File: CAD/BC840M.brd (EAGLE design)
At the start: 25.5 x 40 mm, 79 parts, among them J1 SM02B-SRSS-TB(LF)(SN), U2 BC840M, U3 LP5907MFX-3.3/NOPB, U4 LP5907MFX-3.3/NOPB, U5 ADS131M08IPBS, X1 ABM3B-8.000MHZ-B2-T, X2 FC-12M

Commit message: Update BC840M.brd
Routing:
- net GND: vias 26 -> 27
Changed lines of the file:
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@@
 <wire x1="22.0208" y1="32.121459375" x2="22.0208" y2="31.765859375" width="0.1524" layer="1"/>
 <via x="31.968440625" y="31.4071" extent="1-16" drill="0.2"/>
+<via x="20.26158125" y="38.3794" extent="1-16" drill="0.2"/>
 <wire x1="33.683209375" y1="67.39101875" x2="33.578796875" y2="67.39101875" width="0" layer="19" extent="16-16"/>
 <wire x1="33.61181875" y1="68.78828125" x2="32.953959375" y2="68.072" width="0" layer="19" extent="1-1"/>
 <wire x1="29.0550625" y1="58.625734375" x2="30.4217" y2="58.841640625" width="0" layer="19" extent="16-16"/>
 <wire x1="27.3264" y1="34.6328" x2="25.6996" y2="35.3822" width="0" layer="19" extent="1-1"/>
+<wire x1="25.583003125" y1="49.0982" x2="27.4828" y2="48.8269" width="0" layer="19" extent="1-1"/>
 </signal>
 <signal name="XTAL2_2">

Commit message: latest
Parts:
- added C26, C9: 4.7uF, standardparts:0201
- added C27: 0.1uF, standardparts:0201
- added R28, R29: 10kΩ, standardparts:0402
- added SJ2: (no value), jumper:SJ
- R1: value 46.4kΩ -> 10kΩ
- R3, R4: device standardparts:0201 -> standardparts:0603
- moved R1 2.40 mm to (25.2, 35.7), turned to 270 degrees
- moved C8 1.75 mm to (30.8, 57.1)
- moved C5 1.70 mm to (30.9, 56.3)
- moved C14 1.35 mm to (24.2, 36.0)
- moved R4 1.21 mm to (27.7, 36.8), turned to 180 degrees
- moved R2 0.78 mm to (22.1, 56.2)
- moved R3 0.69 mm to (30.7, 34.4)
- moved C19 0.54 mm to (18.0, 36.9)
- moved C18 0.48 mm to (17.9, 37.7)
- moved S1 0.44 mm to (27.7, 39.6)
- moved SJ1 0.39 mm to (33.2, 57.4)
- moved U$3 0.38 mm to (19.1, 36.4)
- moved C10 0.35 mm to (28.1, 35.7), turned to 180 degrees
- moved C11 0.29 mm to (30.2, 33.0)
- moved R5 0.28 mm to (13.7, 38.3)
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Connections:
- net P4 renamed CUR_DETECT
- net XTAL1_2 renamed CLKIN
- removed net N$67: U$2.3
- removed net REFIN: U5.14
- removed net TD: U$2.15
- removed net TMR: R1.1
- removed net VDDH: U2.A7
- removed net XTAL2_2: C4.1, U5.22, X1.3
- new net CLKOUT: C4.1, JP3.1, U5.22, X1.3
- net +5V: now also C9.2
- net +5V_ISO: now also C26.2, C27.2
- net AVDD: now also SJ2.1, SJ2.2
- net BAT: now also U$2.3
- net CHG: now also R29.2
- net DIN: now also JP3.19
- net DOUT: now also JP3.17
- net GND: now also C26.1, C27.1, C9.1, JP3.5, R1.1, U$2.15, U5.14; no longer R1.2
- net P101: now also JP2.8
- net P104: now also JP2.10
- net P106: now also JP3.11
- net P107: now also JP2.14
- net P108: now also JP2.13
- net P109: now also JP2.15
- net P11: now also JP2.5
- net P110: now also JP3.18
- net P111: now also JP3.4
- net P113: now also JP3.6
- net P114: now also JP3.8
- net P12: now also JP2.9
- net P14: now also JP2.1
- net P15: now also JP2.2
- net P17: now also JP2.3
- net P19: now also JP2.19
- net P2: now also JP3.14
- net P21: now also JP2.12
- net P22: now also JP2.6
- net P23: now also JP3.13
- net P24: now also JP3.20
- net P25: now also JP2.4
- net P28: now also JP3.2
- net P29: now also JP3.16
- net P3: now also JP3.9
- net P30: now also JP3.7
- net P31: now also JP3.12
- net P5: now also JP3.10
- net P7: now also JP2.11
- net P8: now also JP2.7
- net PGOOD: now also R28.2
- net RESET: now also JP2.17
- net SCLK: now also JP3.15
- net SWDCLK: now also JP2.18
- net SWDIO: now also JP2.16
- net SWO: now also JP2.20
- net TS: now also R1.2
- net VDD: now also R28.1, R29.1, U2.A7
- net VIN: now also JP3.3
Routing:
- net GND: track 97.3 -> 129.2 mm
- net VDD: track 58.4 -> 80.7 mm
- net CLKOUT: track 0.00 -> 18.5 mm, vias 0 -> 1
- net XTAL2_2: track 16.8 -> 0.00 mm, vias 1 -> 0
- net P11: track 13.2 -> 18.9 mm
- net BAT: track 26.1 -> 30.0 mm
- net VIN: track 50.7 -> 46.9 mm
- net TS: track 0.00 -> 3.38 mm
- net +5V_ISO: track 66.5 -> 69.5 mm
- net VSWITCH: track 29.0 -> 26.1 mm
- net P7: track 6.62 -> 8.50 mm
- net P113: track 20.1 -> 22.0 mm
- net P114: track 15.5 -> 17.2 mm
- net SCLK: track 29.5 -> 31.1 mm
- net P21: track 22.1 -> 23.7 mm
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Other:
- board text added: "R2"
- board text added: "S1"

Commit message: touchups
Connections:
- net VDD: now also JP3.3
- net VIN: no longer JP3.3
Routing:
- net VIN: track 46.9 -> 35.0 mm
- net VDD: track 80.7 -> 85.2 mm, vias 2 -> 3
- net P28: track 26.9 -> 28.5 mm
- net P111: track 26.5 -> 28.0 mm
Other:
- board text added: "101"
- board text added: "104"
- board text added: "106"
- board text added: "107"
- board text added: "108"
- board text added: "109"
- board text added: "11"
- board text added: "110"
- board text added: "111"
- board text added: "113"
- board text added: "114"
- board text added: "12"
- board text added: "14"
- board text added: "15"
- board text added: "17"
- board text added: "19"
- board text added: "2"
- board text added: "21"
- board text added: "22"
- board text added: "23"
- board text added: "24"
- board text added: "25"
- board text added: "28"
- board text added: "29"
- board text added: "3"
- board text added: "30"
- board text added: "31"
- board text added: "5"
- board text added: "7"
- board text added: "8"
- board text added: "8.192M"
- board text added: "BC840M"
- board text added: "DIN"
- board text added: "DOUT"
- board text added: "SCLK"
- board text added: "SWD CLK"
- board text added: "SWD IO"

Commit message: Update BC840M.brd
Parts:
- moved R6 0.36 mm to (22.4, 40.9)
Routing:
- net GND: track 129.2 -> 158.6 mm

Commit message: _
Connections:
- removed net N$76: U$2.11
- net VSWITCH: now also U$2.11
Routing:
- net VSWITCH: track 26.1 -> 27.7 mm
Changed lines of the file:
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@@
 <grid distance="0.1" unitdist="mil" unit="mil" style="lines" multiple="1" display="no" altdistance="5" altunitdist="mil" altunit="mil"/>
 <layers>
-<layer number="1" name="Top" color="4" fill="1" visible="no" active="yes"/>
+<layer number="1" name="Top" color="4" fill="1" visible="yes" active="yes"/>
 <layer number="2" name="Route2" color="16" fill="1" visible="no" active="no"/>
 <layer number="3" name="Route3" color="17" fill="1" visible="no" active="no"/>
@@
 <layer number="14" name="Route14" color="22" fill="1" visible="no" active="no"/>
 <layer number="15" name="Route15" color="23" fill="1" visible="no" active="no"/>
-<layer number="16" name="Bottom" color="1" fill="1" visible="yes" active="yes"/>
+<layer number="16" name="Bottom" color="1" fill="1" visible="no" active="yes"/>
 <layer number="17" name="Pads" color="2" fill="1" visible="yes" active="yes"/>
 <layer number="18" name="Vias" color="2" fill="1" visible="yes" active="yes"/>
 <layer number="19" name="Unrouted" color="6" fill="1" visible="yes" active="yes"/>
 <layer number="20" name="Dimension" color="24" fill="1" visible="yes" active="yes"/>
-<layer number="21" name="tPlace" color="7" fill="1" visible="no" active="yes"/>
-<layer number="22" name="bPlace" color="7" fill="1" visible="yes" active="yes"/>
-<layer number="23" name="tOrigins" color="15" fill="1" visible="no" active="yes"/>
-<layer number="24" name="bOrigins" color="15" fill="1" visible="yes" active="yes"/>
-<layer number="25" name="tNames" color="7" fill="1" visible="no" active="yes"/>
-<layer number="26" name="bNames" color="7" fill="1" visible="yes" active="yes"/>
+<layer number="21" name="tPlace" color="7" fill="1" visible="yes" active="yes"/>
+<layer number="22" name="bPlace" color="7" fill="1" visible="no" active="yes"/>
+<layer number="23" name="tOrigins" color="15" fill="1" visible="yes" active="yes"/>
+<layer number="24" name="bOrigins" color="15" fill="1" visible="no" active="yes"/>
+<layer number="25" name="tNames" color="7" fill="1" visible="yes" active="yes"/>
+<layer number="26" name="bNames" color="7" fill="1" visible="no" active="yes"/>
 <layer number="27" name="tValues" color="7" fill="1" visible="no" active="yes"/>
 <layer number="28" name="bValues" color="7" fill="1" visible="no" active="yes"/>
@@
 <layer number="37" name="tTest" color="7" fill="1" visible="no" active="yes"/>
 <layer number="38" name="bTest" color="7" fill="1" visible="no" active="yes"/>
-<layer number="39" name="tKeepout" color="4" fill="11" visible="no" active="yes"/>
-<layer number="40" name="bKeepout" color="1" fill="11" visible="yes" active="yes"/>
-<layer number="41" name="tRestrict" color="4" fill="10" visible="no" active="yes"/>
-<layer number="42" name="bRestrict" color="1" fill="10" visible="yes" active="yes"/>
+<layer number="39" name="tKeepout" color="4" fill="11" visible="yes" active="yes"/>
+<layer number="40" name="bKeepout" color="1" fill="11" visible="no" active="yes"/>
+<layer number="41" name="tRestrict" color="4" fill="10" visible="yes" active="yes"/>
+<layer number="42" name="bRestrict" color="1" fill="10" visible="no" active="yes"/>
 <layer number="43" name="vRestrict" color="2" fill="10" visible="no" active="yes"/>
 <layer number="44" name="Drills" color="7" fill="1" visible="no" active="yes"/>
@@
 <layer number="49" name="Reference" color="7" fill="1" visible="no" active="yes"/>
 <layer number="50" name="dxf" color="7" fill="1" visible="no" active="yes"/>
-<layer number="51" name="tDocu" color="7" fill="1" visible="no" active="yes"/>
-<layer number="52" name="bDocu" color="7" fill="1" visible="yes" active="yes"/>
+<layer number="51" name="tDocu" color="7" fill="1" visible="yes" active="yes"/>
+<layer number="52" name="bDocu" color="7" fill="1" visible="no" active="yes"/>
 <layer number="53" name="tGND_GNDA" color="7" fill="9" visible="no" active="no"/>
 <layer number="54" name="bGND_GNDA" color="1" fill="9" visible="no" active="no"/>
@@
 <wire x1="24.429725" y1="35.351840625" x2="24.429725" y2="33.9478" width="0.1524" layer="1"/>
 </signal>
-<signal name="N$76">
-<contactref element="U$2" pad="11"/>
-</signal>
 <signal name="ILM">
 <contactref element="R3" pad="2"/>
@@
 <wire x1="26.138528125" y1="31.086421875" x2="26.666671875" y2="31.086421875" width="0.1524" layer="1"/>
 <wire x1="28.5114" y1="32.9478" x2="29.89991875" y2="32.9478" width="0.254" layer="1"/>
+<contactref element="U$2" pad="11"/>
+<wire x1="28.5114" y1="33.4478" x2="29.39991875" y2="33.4478" width="0.254" layer="1"/>
+<wire x1="29.39991875" y1="33.4478" x2="29.89991875" y2="32.9478" width="0.254" layer="1"/>
 </signal>
 <signal name="+5V_ISO">

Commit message: latest
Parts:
- moved U$2 0.41 mm to (27.3, 33.5)
- moved C10 0.32 mm to (28.4, 35.9)
- moved R1 0.21 mm to (25.2, 35.9)
- moved R4 0.21 mm to (27.7, 37.0)
- moved C14 0.20 mm to (24.2, 36.2)
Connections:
- new net AVDD1: SJ2.1, U4.5
- new net TMR: U$2.14
- net AVDD: no longer SJ2.1, U4.5
- net GND: now also U$2.6; no longer U$2.14, U$2.5
- net P11: now also JP2.7; no longer JP2.5
- net P8: now also JP2.5; no longer JP2.7
- net VSWITCH: now also U$2.5; no longer U$2.6
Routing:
- net P11: track 18.9 -> 14.6 mm
- net GND: track 158.6 -> 161.5 mm, vias 27 -> 28
- net AVDD1: track 0.00 -> 2.64 mm
- net P8: track 12.8 -> 15.1 mm
- net AVDD: track 8.69 -> 6.52 mm
- net VSWITCH: track 27.7 -> 26.6 mm
- net BAT: track 30.0 -> 29.0 mm
- net PGOOD: track 40.2 -> 41.2 mm
- net CUR_DETECT: track 30.0 -> 29.2 mm
- net ILM: track 1.97 -> 1.31 mm
- net RESET: track 31.3 -> 30.7 mm
- net P26: track 31.3 -> 30.8 mm

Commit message: still need to add TVS diodes
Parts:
- added R30, R31: 100kΩ, standardparts:0402
- moved DOUT 0.56 mm to (35.7, 65.9)
- moved DRDY 0.36 mm to (35.7, 64.3)
- moved SCLK 0.27 mm to (36.0, 65.1)
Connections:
- net CS: now also R31.1
- net DOUT: now also R30.1
- net GND: now also R30.2
- net VDD: now also R31.2
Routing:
- net VDD: track 85.2 -> 86.3 mm

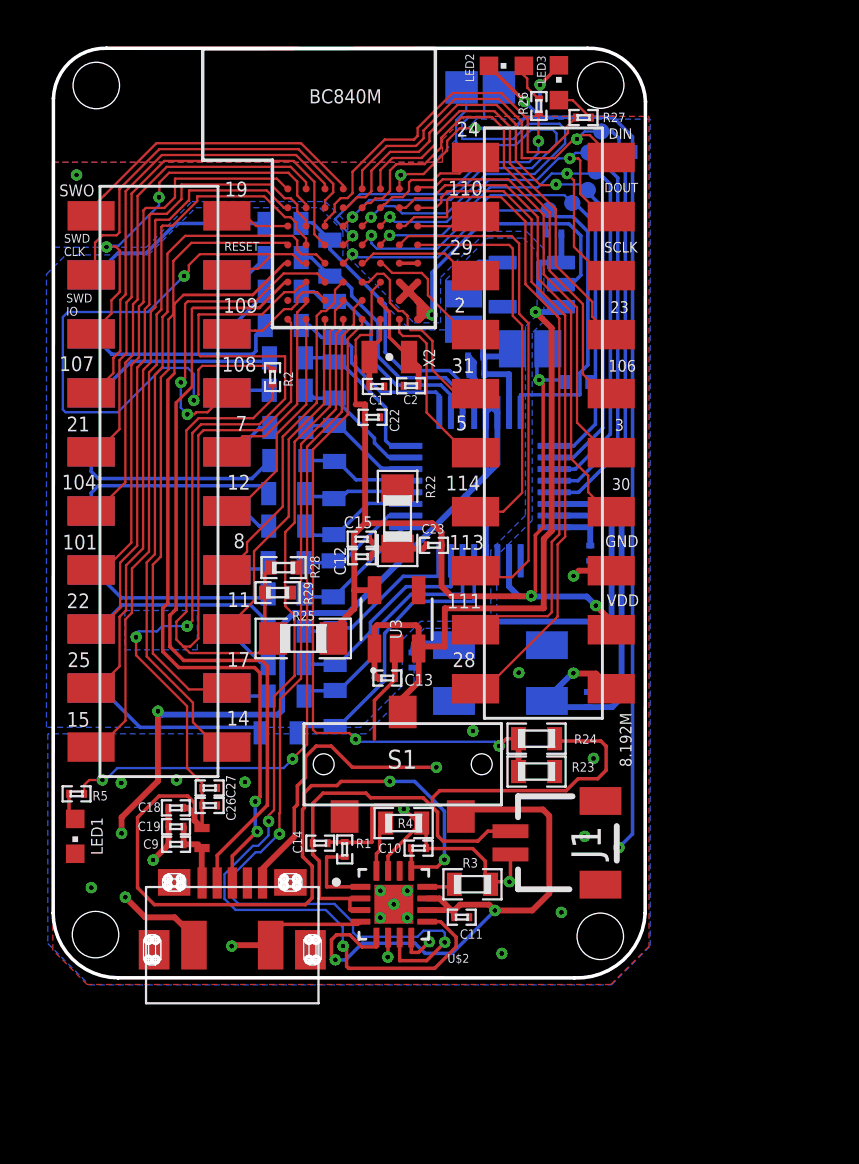
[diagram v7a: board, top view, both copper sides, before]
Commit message: fixed a ground
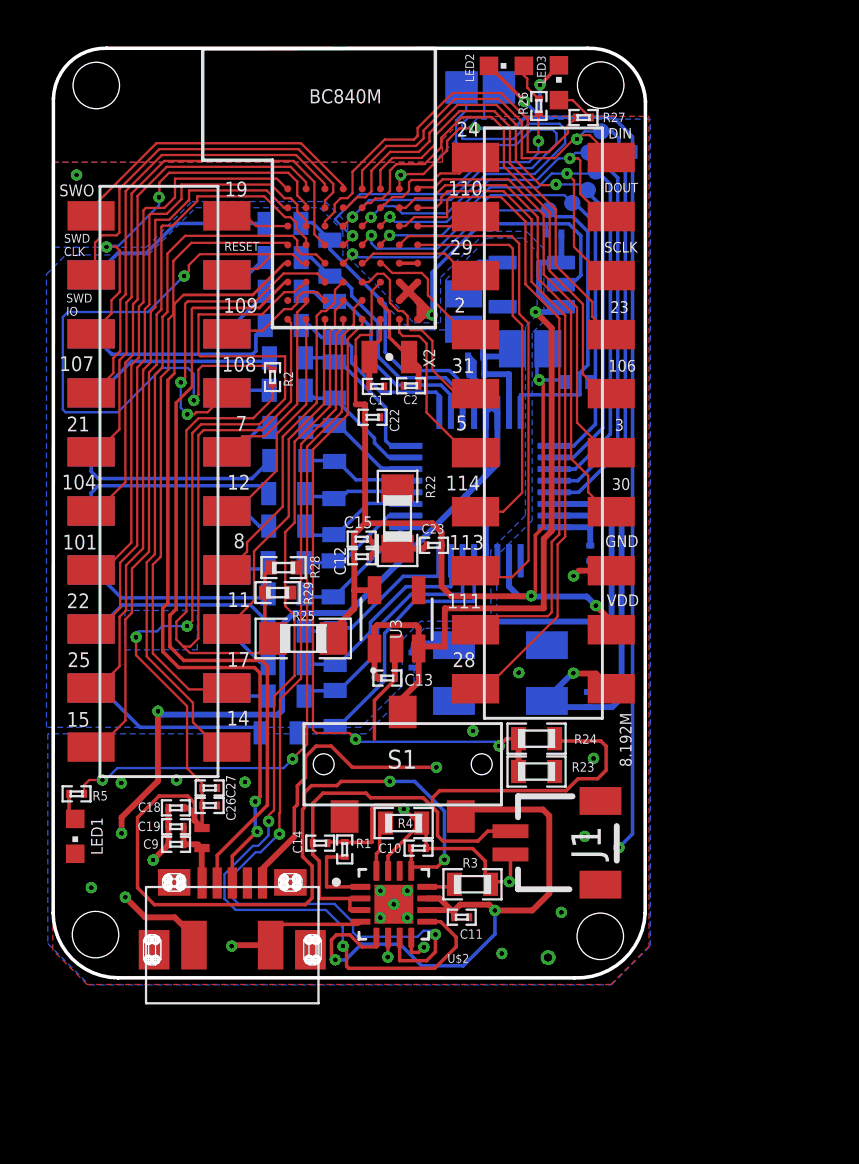
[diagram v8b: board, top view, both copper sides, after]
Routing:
- net VSWITCH: track 26.6 -> 27.6 mm
- net PGOOD: track 41.2 -> 40.7 mm
- net GND: track 161.6 -> 161.3 mm, vias 28 -> 29
